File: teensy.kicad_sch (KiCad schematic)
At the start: 5 parts, among them J3 HFJ11-2450E-L12RL, U1 Teensy4.1

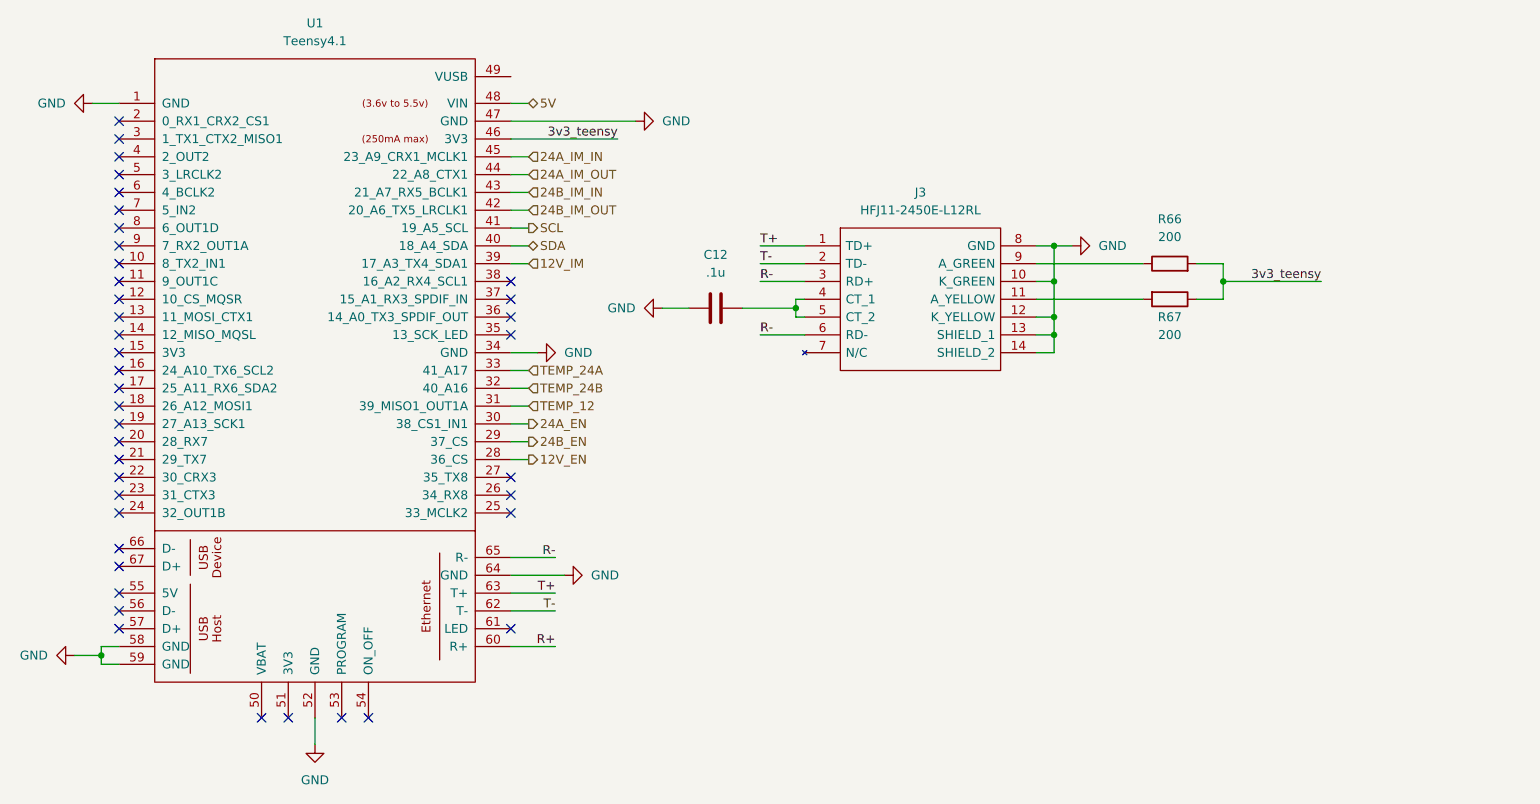
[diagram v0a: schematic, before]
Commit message: fixed 5 buck aux
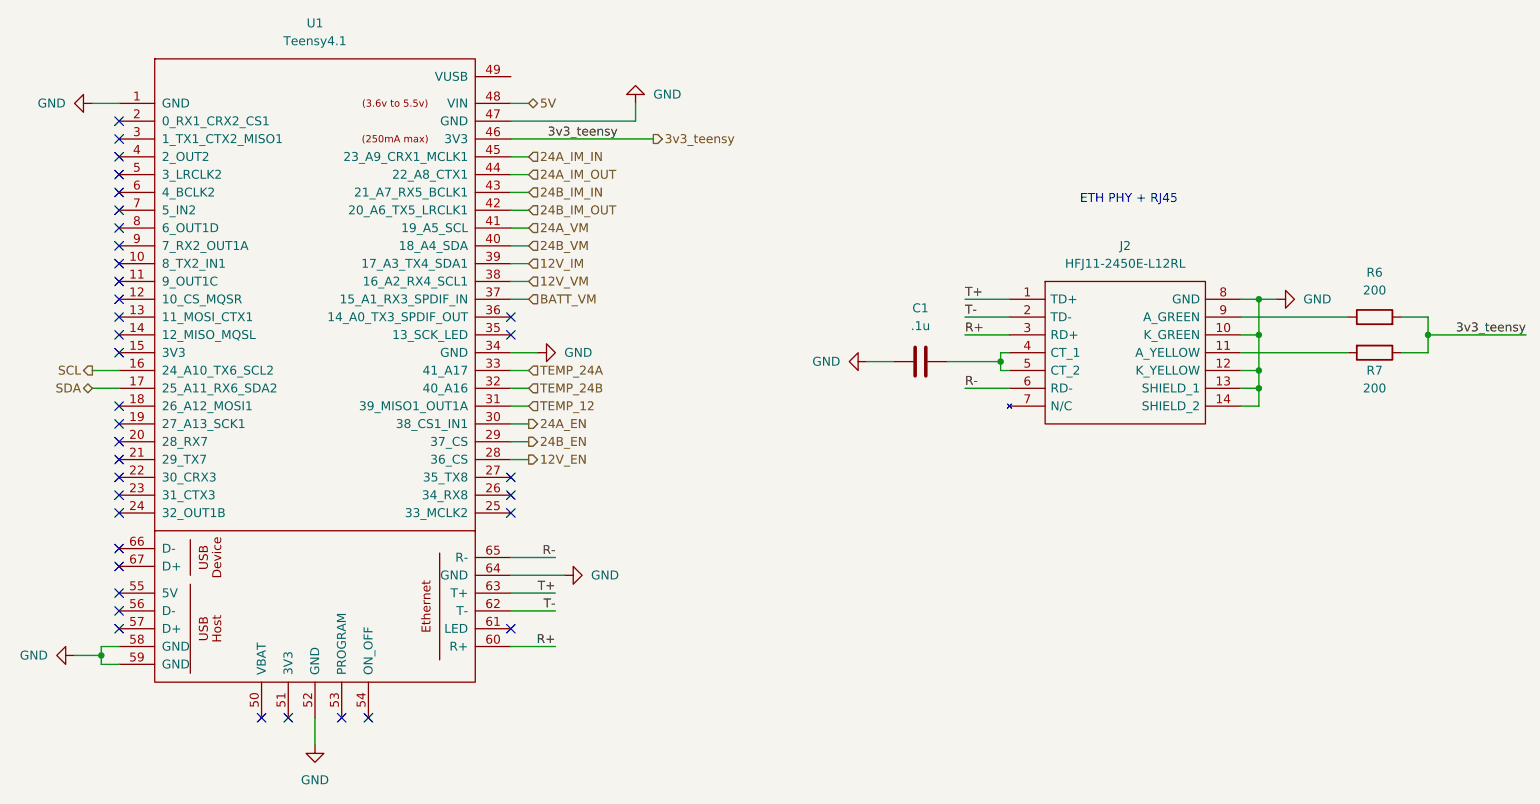
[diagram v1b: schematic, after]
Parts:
- C1: renamed from C12; footprint (none) -> Capacitor_SMD:C_0603_1608Metric
- J2: renamed from J3; footprint HFJ112450EL12RL -> (none)
- R6: renamed from R66; footprint (none) -> Resistor_SMD:R_0603_1608Metric
- R7: renamed from R67; footprint (none) -> Resistor_SMD:R_0603_1608Metric
- U1: footprint (none) -> power_dist:Teensy41
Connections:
- net R+: now also J2.3 (RD+)
- net R-: no longer J2.3 (RD+)
- net SCL: now also U1.16 (24_A10_TX6_SCL2); no longer U1.41 (19_A5_SCL)
- net SDA: now also U1.17 (25_A11_RX6_SDA2); no longer U1.40 (18_A4_SDA)
- net BATT_VM: now reaches U1.37 (15_A1_RX3_SPDIF_IN)
- net 12V_VM: now reaches U1.38 (16_A2_RX4_SCL1)
- new net 24A_VM: U1.41 (19_A5_SCL)
- new net 24B_VM: U1.40 (18_A4_SDA)
- no-connect marks 40 -> 36
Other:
- note added: "ETH PHY + RJ45"
- moved on the sheet: C1, J2, R6, R7

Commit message: assigned footprints
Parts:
- J2: footprint (none) -> power_dist:HFJ112450EL12RL
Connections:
- net TEMP_24A: now also U1.27 (35_TX8); no longer U1.33 (41_A17)
- net TEMP_24B: now also U1.26 (34_RX8); no longer U1.32 (40_A16)
- net OC_n: now reaches U1.25 (33_MCLK2)
- new net BAT_IM_VOUT: U1.33 (41_A17)
- new net BAT_IM_VREF: U1.32 (40_A16)
- no-connect marks 36 -> 34
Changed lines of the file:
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@@
-	)
-	(no_connect
-		(at 124.46 107.95)
 	)
 	(no_connect
@@
 	)
 	(no_connect
-		(at 124.46 105.41)
+		(at 124.46 48.26)
 	)
 	(no_connect
@@
 	)
 	(no_connect
-		(at 124.46 110.49)
-	)
-	(no_connect
 		(at 68.58 59.69)
 	)
@@
 	(wire
 		(pts
+			(xy 127 105.41) (xy 124.46 105.41)
+		)
+		(stroke
+			(width 0)
+			(type default)
+		)
+	)
+	(wire
+		(pts
 			(xy 194.31 87.63) (xy 194.31 88.9)
 		)
@@
 		(pts
 			(xy 251.46 82.55) (xy 255.27 82.55)
+		)
+		(stroke
+			(width 0)
+			(type default)
+		)
+	)
+	(wire
+		(pts
+			(xy 127 107.95) (xy 124.46 107.95)
+		)
+		(stroke
+			(width 0)
+			(type default)
+		)
+	)
+	(wire
+		(pts
+			(xy 124.46 110.49) (xy 127 110.49)
 		)
 		(stroke
@@
 		)
 	)
+	(hierarchical_label "TEMP_24A"
+		(shape input)
+		(at 127 105.41 0)
+		(effects
+			(font
+				(size 1.27 1.27)
+			)
+			(justify left)
+		)
+	)
 	(hierarchical_label "24A_IM_OUT"
 		(shape input)
@@
 		)
 	)
+	(hierarchical_label "TEMP_24B"
+		(shape input)
+		(at 127 107.95 0)
+		(effects
+			(font
+				(size 1.27 1.27)
+			)
+			(justify left)
+		)
+	)
 	(hierarchical_label "12V_EN"
 		(shape output)
@@
 		)
 	)
+	(hierarchical_label "BAT_IM_VOUT"
+		(shape input)
+		(at 127 90.17 0)
+		(effects
+			(font
+				(size 1.27 1.27)
+			)
+			(justify left)
+		)
+	)
 	(hierarchical_label "TEMP_12"
 		(shape input)
@@
 		)
 	)
+	(hierarchical_label "BAT_IM_VREF"
+		(shape input)
+		(at 127 92.71 0)
+		(effects
+			(font
+				(size 1.27 1.27)
+			)
+			(justify left)
+		)
+	)
 	(hierarchical_label "24B_IM_IN"
 		(shape input)
@@
 		)
 	)
-	(hierarchical_label "TEMP_24A"
+	(hierarchical_label "OC_n"
 		(shape input)
-		(at 127 90.17 0)
-		(effects
-			(font
-				(size 1.27 1.27)
-			)
-			(justify left)
-		)
-	)
-	(hierarchical_label "TEMP_24B"
-		(shape input)
-		(at 127 92.71 0)
+		(at 127 110.49 0)
 		(effects
 			(font
@@
 			)
 		)
-		(property "Footprint" ""
+		(property "Footprint" "power_dist:HFJ112450EL12RL"
 			(at 224.79 77.47 0)
 			(hide yes)
